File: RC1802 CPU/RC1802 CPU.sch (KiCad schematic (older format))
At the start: 50 parts, among them J1 Mount, J2 Mount, J3 Mount, J4 Mount, J5 CONN_01X39, J6 CONN_02X20, J7 BARREL_JACK, J8 Conn_CLK, J9 Conn_Q, U1 74LS04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

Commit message: Fixed label snafoos
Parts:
- removed J8: Conn_CLK, Pin_Headers:Pin_Header_Straight_1x05_Pitch2.54mm, symbol Conn_01x05
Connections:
- net labels removed: CLEAR, LOAD, RUN, WAIT, ~WE
- wire segments 224 -> 197
- no-connect marks 12 -> 24
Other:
- moved on the sheet: R4, R5, R6, R7, U1C, U1D, U1E, U1F, X1

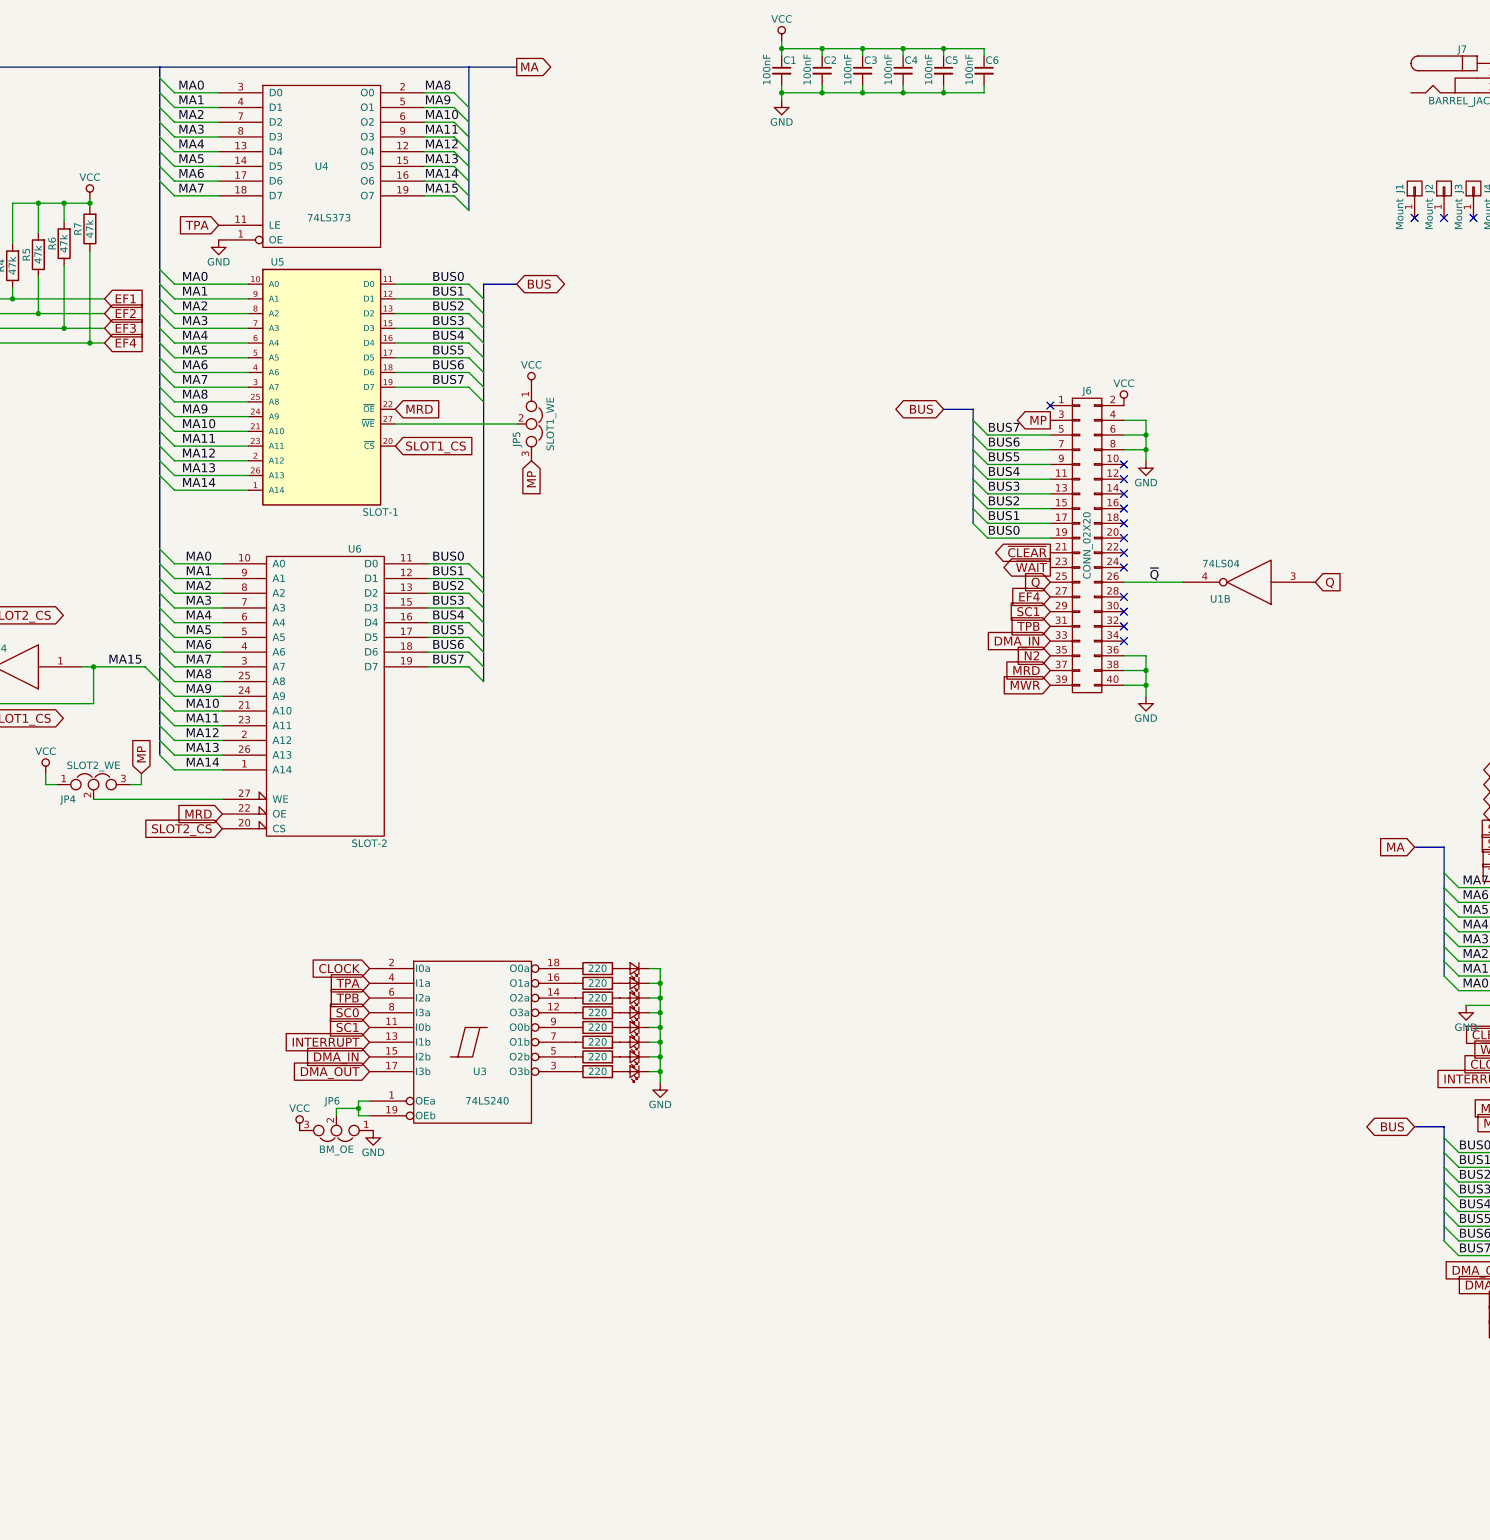
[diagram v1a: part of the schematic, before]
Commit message: Fixed tracks missing due to labelling issues
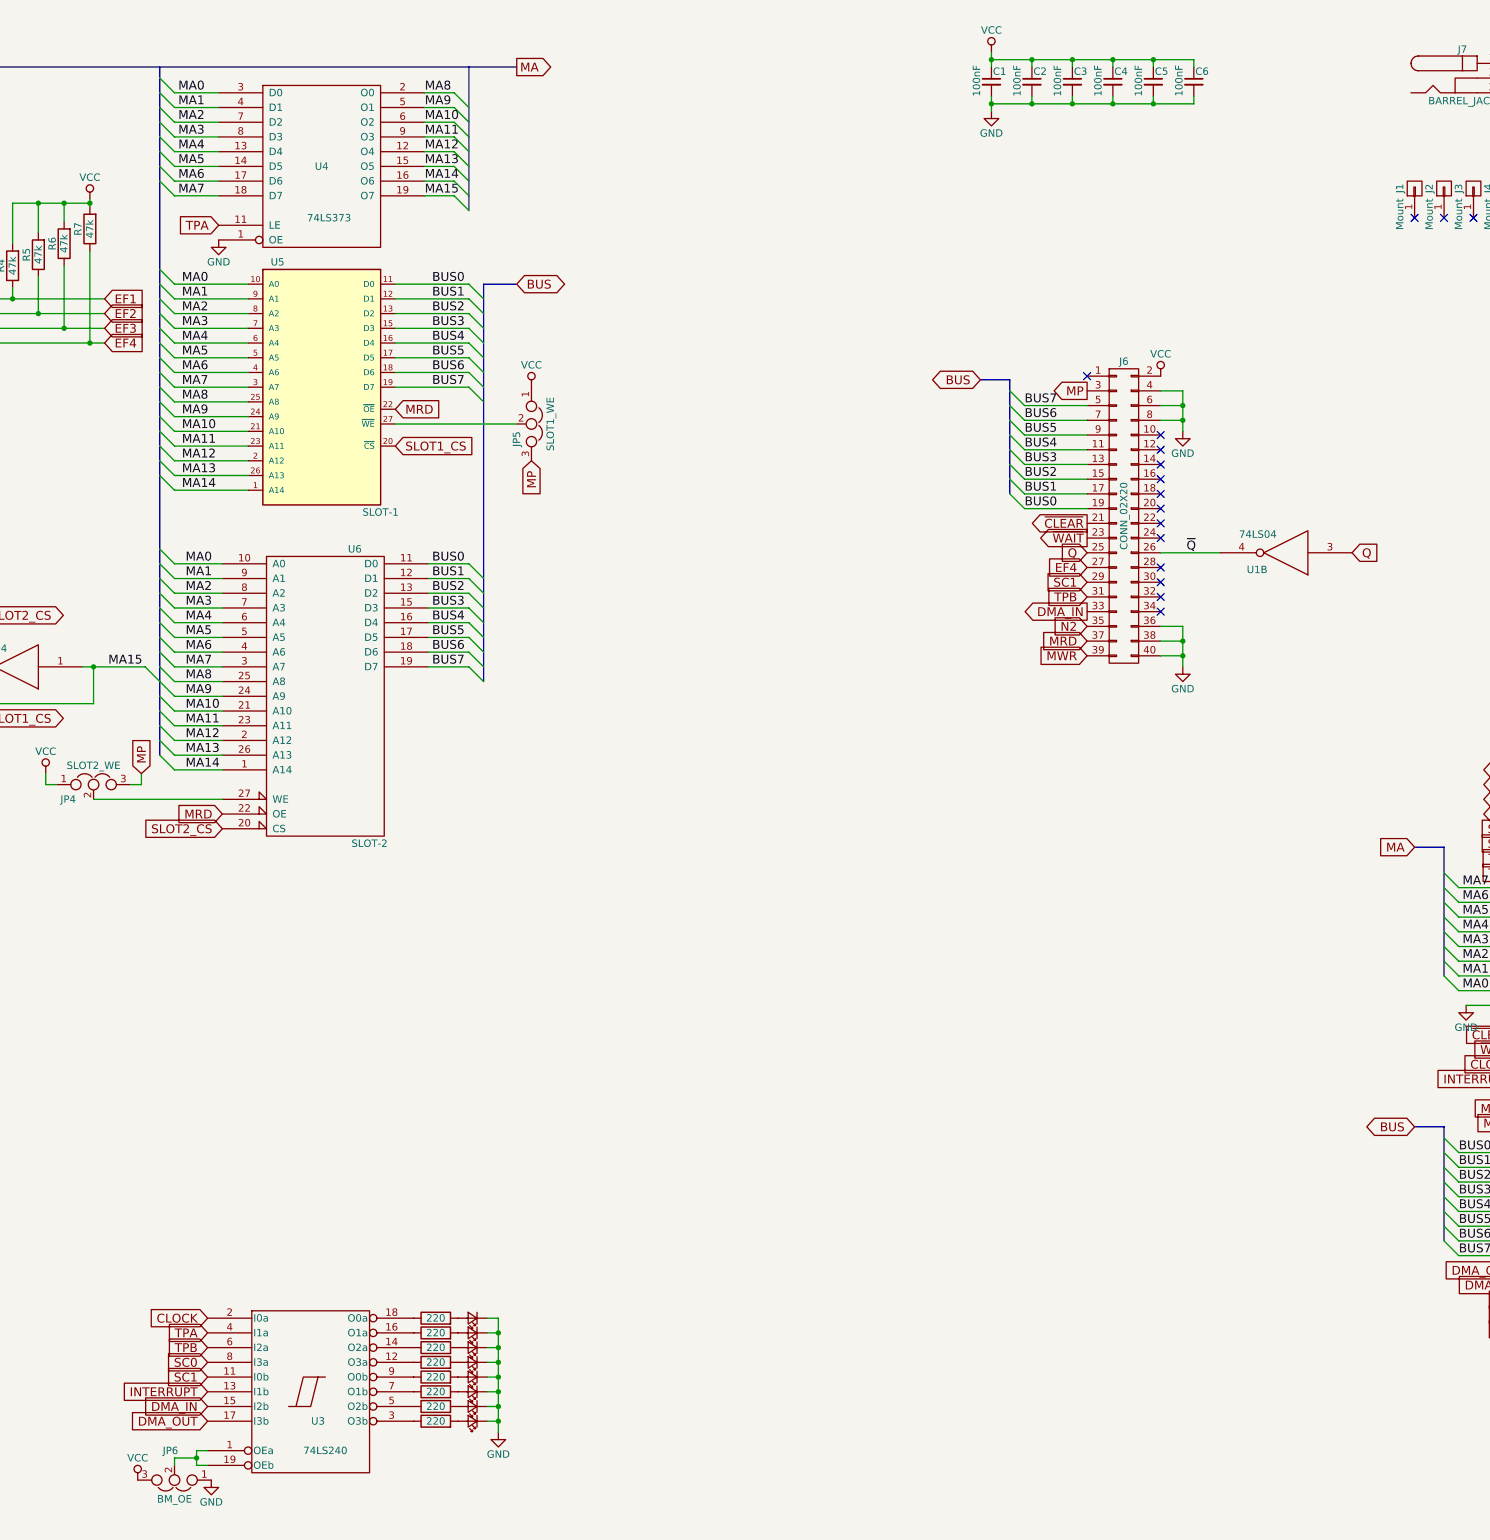
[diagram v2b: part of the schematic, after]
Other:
- moved on the sheet: C1, C2, C3, C4, C5, C6, J6, JP6, U1B, U3

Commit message: Gerber export CPU board after adding clockport
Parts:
- added J8: ClockPort, Pin_Headers:Pin_Header_Straight_1x05_Pitch2.54mm, symbol Conn_01x05-RESCUE-RC1802_CPU
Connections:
- net labels added: CLK_PWR
- wire segments 197 -> 205
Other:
- moved on the sheet: X1
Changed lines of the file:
@@
 EESchema Schematic File Version 2
+LIBS:RC1802 CPU-rescue
 LIBS:cdp1802
 LIBS:power
@@
 L CXO_DIP14 X1
 U 1 1 59462D89
-P 1225 1300
-F 0 "X1" H 1025 1550 50  0000 L CNN
-F 1 "CXO_DIP14" H 1275 1050 50  0000 L CNN
-F 2 "Oscillators:Oscillator_DIP-14" H 1675 950 50  0001 C CNN
-F 3 "" H 1125 1300 50  0001 C CNN
-	1    1225 1300
-	0    -1   1    0
+P 1800 1750
+F 0 "X1" H 1600 2000 50  0000 L CNN
+F 1 "CXO_DIP14" H 1850 1500 50  0000 L CNN
+F 2 "Oscillators:Oscillator_DIP-14" H 2250 1400 50  0001 C CNN
+F 3 "" H 1700 1750 50  0001 C CNN
+	1    1800 1750
+	-1   0    0    -1
 $EndComp
 $Comp
 L GND #PWR05
 U 1 1 59462F59
-P 1625 1400
-F 0 "#PWR05" H 1625 1150 50  0001 C CNN
-F 1 "GND" H 1625 1250 50  0000 C CNN
-F 2 "" H 1625 1400 50  0001 C CNN
-F 3 "" H 1625 1400 50  0001 C CNN
-	1    1625 1400
+P 1900 1075
+F 0 "#PWR05" H 1900 825 50  0001 C CNN
+F 1 "GND" H 1900 925 50  0000 C CNN
+F 2 "" H 1900 1075 50  0001 C CNN
+F 3 "" H 1900 1075 50  0001 C CNN
+	1    1900 1075
 	1    0    0    -1
 $EndComp
@@
 	1    0    0    -1
 $EndComp
-NoConn ~ 1225 1000
+NoConn ~ 2100 1750
 Text GLabel 15575 5900 0    60   Output ~ 0
 EF1
@@
 Text Label 8125 2000 0    60   ~ 0
 MA15
-Text GLabel 1225 1600 3    60   Output ~ 0
+Text GLabel 1500 1175 0    60   Output ~ 0
 CLOCK
 Text GLabel 3425 1550 0    60   Input ~ 0
@@
 L VCC #PWR024
 U 1 1 5BA993FE
-P 825 1200
-F 0 "#PWR024" H 825 1050 50  0001 C CNN
-F 1 "VCC" H 825 1350 50  0000 C CNN
-F 2 "" H 825 1200 50  0001 C CNN
-F 3 "" H 825 1200 50  0001 C CNN
-	1    825  1200
-	1    0    0    -1
-$EndComp
-Wire Wire Line
-	825  1200 825  1300
-Wire Wire Line
-	825  1300 925  1300
-Wire Wire Line
-	1525 1300 1625 1300
-Wire Wire Line
-	1625 1300 1625 1400
+P 2350 950
+F 0 "#PWR024" H 2350 800 50  0001 C CNN
+F 1 "VCC" H 2350 1100 50  0000 C CNN
+F 2 "" H 2350 950 50  0001 C CNN
+F 3 "" H 2350 950 50  0001 C CNN
+	1    2350 950
+	1    0    0    -1
+$EndComp
 Wire Wire Line
 	925  2825 925  2900
 Wire Wire Line
 	925  2825 1150 2825
+$Comp
+L Conn_01x05-RESCUE-RC1802_CPU J8
+U 1 1 5BA8B962
+P 1900 825
+F 0 "J8" H 1900 1125 50  0000 C CNN
+F 1 "ClockPort" H 1900 525 50  0000 C CNN
+F 2 "Pin_Headers:Pin_Header_Straight_1x05_Pitch2.54mm" H 1900 825 50  0001 C CNN
+F 3 "" H 1900 825 50  0001 C CNN
+	1    1900 825
+	0    -1   -1   0
+$EndComp
+Wire Wire Line
+	1800 1450 1800 1400
+Wire Wire Line
+	1800 1400 2000 1400
+Wire Wire Line
+	2000 1400 2000 1025
+Wire Wire Line
+	1500 1750 1500 1300
+Wire Wire Line
+	1500 1300 1800 1300
+Wire Wire Line
+	1800 1300 1800 1025
+Wire Wire Line
+	1500 1175 1700 1175
+Wire Wire Line
+	1700 1175 1700 1025
+Wire Wire Line
+	2350 950  2350 1175
+Wire Wire Line
+	2350 1175 2100 1175
+Wire Wire Line
+	2100 1175 2100 1025
+$Comp
+L GND #PWR025
+U 1 1 5BA8D417
+P 1800 2050
+F 0 "#PWR025" H 1800 1800 50  0001 C CNN
+F 1 "GND" H 1800 1900 50  0000 C CNN
+F 2 "" H 1800 2050 50  0001 C CNN
+F 3 "" H 1800 2050 50  0001 C CNN
+	1    1800 2050
+	1    0    0    -1
+$EndComp
+Text Label 1975 1400 2    60   ~ 0
+CLK_PWR
+Wire Wire Line
+	1900 1075 1900 1025
 $EndSCHEMATC

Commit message: Added jumpers for inverting TX/RX
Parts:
- removed J9: Conn_Q, Pin_Headers:Pin_Header_Angled_1x04_Pitch2.54mm, symbol Conn_01x04
- added D9: 1N4148, Diodes_THT:D_DO-35_SOD27_P7.62mm_Horizontal, symbol D
- added J9: Q_Connector, Pin_Headers:Pin_Header_Angled_1x05_Pitch2.54mm, symbol Conn_01x05_Male
- added JP1: RX_SEL, Pin_Headers:Pin_Header_Straight_1x03_Pitch2.54mm, symbol Jumper_NC_Dual
- added JP7: RX_INVERT, Pin_Headers:Pin_Header_Straight_1x03_Pitch2.54mm, symbol Jumper_NC_Dual
- added JP8: TX_INVERT, Pin_Headers:Pin_Header_Straight_1x03_Pitch2.54mm, symbol Jumper_NC_Dual
- J5: value CONN_01X39 -> Expansion
- J6: value CONN_02X20 -> UI_Connector
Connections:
- net labels added: RX, TX
- wire segments 205 -> 225
- no-connect marks 24 -> 23
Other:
- moved on the sheet: U1B, U1C
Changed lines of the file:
@@
 P 15775 7800
 F 0 "J5" H 15775 9800 50  0000 C CNN
-F 1 "CONN_01X39" V 15875 7800 50  0000 C CNN
+F 1 "Expansion" V 15875 7800 50  0000 C CNN
 F 2 "Pin_Headers:Pin_Header_Angled_1x39_Pitch2.54mm" H 15775 7800 50  0001 C CNN
 F 3 "" H 15775 7800 50  0001 C CNN
@@
 P 12875 4175
 F 0 "J6" H 12875 5225 50  0000 C CNN
-F 1 "CONN_02X20" V 12875 4175 50  0000 C CNN
+F 1 "UI_Connector" V 12875 4175 50  0000 C CNN
 F 2 "Pin_Headers:Pin_Header_Straight_2x20_Pitch2.54mm" H 12875 3225 50  0001 C CNN
 F 3 "" H 12875 3225 50  0001 C CNN
@@
 L 74LS04 U1
 U 2 1 5B22F8BE
-P 13975 4425
-F 0 "U1" H 14170 4540 50  0000 C CNN
-F 1 "74LS04" H 14165 4300 50  0000 C CNN
-F 2 "Housings_DIP:DIP-14_W7.62mm_Socket" H 13975 4425 50  0001 C CNN
-F 3 "" H 13975 4425 50  0001 C CNN
-	2    13975 4425
-	-1   0    0    1
+P 4050 8775
+F 0 "U1" H 4245 8890 50  0000 C CNN
+F 1 "74LS04" H 4240 8650 50  0000 C CNN
+F 2 "Housings_DIP:DIP-14_W7.62mm_Socket" H 4050 8775 50  0001 C CNN
+F 3 "" H 4050 8775 50  0001 C CNN
+	2    4050 8775
+	1    0    0    -1
 $EndComp
 $Comp
 L 74LS04 U1
 U 3 1 5B22F92F
-P 1175 9400
-F 0 "U1" H 1370 9515 50  0000 C CNN
-F 1 "74LS04" H 1365 9275 50  0000 C CNN
-F 2 "Housings_DIP:DIP-14_W7.62mm_Socket" H 1175 9400 50  0001 C CNN
-F 3 "" H 1175 9400 50  0001 C CNN
-	3    1175 9400
+P 4050 7075
+F 0 "U1" H 4245 7190 50  0000 C CNN
+F 1 "74LS04" H 4240 6950 50  0000 C CNN
+F 2 "Housings_DIP:DIP-14_W7.62mm_Socket" H 4050 7075 50  0001 C CNN
+F 3 "" H 4050 7075 50  0001 C CNN
+	3    4050 7075
 	-1   0    0    1
 $EndComp
@@
 	-1   0    0    1
 $EndComp
-NoConn ~ 725  9400
 NoConn ~ 725  9800
 NoConn ~ 725  10200
@@
 	1    0    0    -1
 $EndComp
-$Comp
-L Conn_01x04 J9
-U 1 1 5B6A11D6
-P 1350 3100
-F 0 "J9" H 1350 3200 50  0000 C CNN
-F 1 "Conn_Q" H 1350 2900 50  0000 C CNN
-F 2 "Pin_Headers:Pin_Header_Angled_1x04_Pitch2.54mm" H 1350 3100 50  0001 C CNN
-F 3 "" H 1350 3100 50  0001 C CNN
-	1    1350 3100
-	0    1    1    0
-$EndComp
-Text GLabel 1450 2825 1    60   Input ~ 0
+Text GLabel 1500 7275 3    60   Input ~ 0
 Q
 $Comp
 L GND #PWR021
 U 1 1 5B6A17C7
-P 925 2900
-F 0 "#PWR021" H 925 2650 50  0001 C CNN
-F 1 "GND" H 925 2750 50  0000 C CNN
-F 2 "" H 925 2900 50  0001 C CNN
-F 3 "" H 925 2900 50  0001 C CNN
-	1    925  2900
-	1    0    0    -1
+P 925 7175
+F 0 "#PWR021" H 925 6925 50  0001 C CNN
+F 1 "GND" H 925 7025 50  0000 C CNN
+F 2 "" H 925 7175 50  0001 C CNN
+F 3 "" H 925 7175 50  0001 C CNN
+	1    925  7175
+	-1   0    0    1
 $EndComp
 $Comp
 L VCC #PWR022
 U 1 1 5B6A3EEC
-P 1350 2625
-F 0 "#PWR022" H 1350 2475 50  0001 C CNN
-F 1 "VCC" H 1350 2775 50  0000 C CNN
-F 2 "" H 1350 2625 50  0001 C CNN
-F 3 "" H 1350 2625 50  0001 C CNN
-	1    1350 2625
-	1    0    0    -1
-$EndComp
-Text GLabel 1250 2825 1    60   Output ~ 0
-EF3
+P 1600 7425
+F 0 "#PWR022" H 1600 7275 50  0001 C CNN
+F 1 "VCC" H 1600 7575 50  0000 C CNN
+F 2 "" H 1600 7425 50  0001 C CNN
+F 3 "" H 1600 7425 50  0001 C CNN
+	1    1600 7425
+	-1   0    0    1
+$EndComp
 Wire Wire Line
 	4825 1600 4950 1600
@@
 	11975 1375 13350 1375
 Wire Wire Line
-	1775 9400 1775 10850
+	1775 9800 1775 10850
 Wire Wire Line
 	1775 10600 1625 10600
@@
 Connection ~ 1775 10200
 Wire Wire Line
-	1625 9800 1775 9800
-Connection ~ 1775 9800
-Wire Wire Line
 	7925 3550 8750 3550
 Wire Wire Line
@@
 	5550 6000 5550 5925
 Wire Wire Line
-	1450 2825 1450 2900
-Wire Wire Line
-	1150 2825 1150 2900
-Wire Wire Line
-	1350 2900 1350 2625
-Wire Wire Line
-	1250 2900 1250 2825
-Wire Wire Line
-	13125 4425 13525 4425
-Text GLabel 14425 4425 2    60   Input ~ 0
+	1600 7150 1600 7425
+Text GLabel 3350 8400 0    60   Input ~ 0
 Q
-Wire Wire Line
-	1625 9400 1775 9400
-Text Label 13300 4425 0    60   ~ 0
-~Q
 Wire Wire Line
 	13275 5125 13125 5125
@@
 $EndComp
 Wire Wire Line
-	925  2825 925  2900
-Wire Wire Line
-	925  2825 1150 2825
+	925  7250 925  7175
 $Comp
 L Conn_01x05-RESCUE-RC1802_CPU J8
@@
 Wire Wire Line
 	1900 1075 1900 1025
+Text GLabel 4850 8775 2    60   Output ~ 0
+~Q
+Text GLabel 13125 4425 2    60   Input ~ 0
+~Q
+Wire Wire Line
+	3350 8400 3500 8400
+$Comp
+L Jumper_NC_Dual JP1
+U 1 1 5BB50981
+P 2725 7450
+F 0 "JP1" H 2775 7350 50  0000 L CNN
+F 1 "RX_SEL" H 2725 7550 50  0000 C BNN
+F 2 "Pin_Headers:Pin_Header_Straight_1x03_Pitch2.54mm" H 2725 7450 50  0001 C CNN
+F 3 "" H 2725 7450 50  0001 C CNN
+	1    2725 7450
+	0    -1   -1   0
+$EndComp
+Text GLabel 2600 7075 0    60   Output ~ 0
+EF3
+Text GLabel 2600 7825 0    60   Output ~ 0
+EF4
+$Comp
+L D D9
+U 1 1 5BB522A5
+P 3100 7450
+F 0 "D9" H 3100 7550 50  0000 C CNN
+F 1 "1N4148" H 3100 7350 50  0000 C CNN
+F 2 "Diodes_THT:D_DO-35_SOD27_P7.62mm_Horizontal" H 3100 7450 50  0001 C CNN
+F 3 "" H 3100 7450 50  0001 C CNN
+	1    3100 7450
+	-1   0    0    1
+$EndComp
+Wire Wire Line
+	2950 7450 2825 7450
+$Comp
+L Jumper_NC_Dual JP7
+U 1 1 5BB52E45
+P 3475 7450
+F 0 "JP7" H 3525 7350 50  0000 L CNN
+F 1 "RX_INVERT" H 3475 7550 50  0000 C BNN
+F 2 "Pin_Headers:Pin_Header_Straight_1x03_Pitch2.54mm" H 3475 7450 50  0001 C CNN
+F 3 "" H 3475 7450 50  0001 C CNN
+	1    3475 7450
+	0    1    1    0
+$EndComp
+Wire Wire Line
+	3250 7450 3375 7450
+Wire Wire Line
+	3475 7200 3475 7075
+Wire Wire Line
+	3475 7075 3600 7075
+Wire Wire Line
+	3475 7700 3475 7825
+Wire Wire Line
+	4625 7825 3475 7825
+Wire Wire Line
+	4625 7075 4625 7825
+Wire Wire Line
+	4625 7075 4500 7075
+Wire Wire Line
+	4625 7450 4750 7450
+Connection ~ 4625 7450
+Wire Wire Line
+	2725 7200 2725 7075
+Wire Wire Line
+	2725 7075 2600 7075
+Wire Wire Line
+	2600 7825 2725 7825
+Wire Wire Line
+	2725 7825 2725 7700
+Text GLabel 4750 7450 2    60   Input ~ 0
+RX
+Wire Wire Line
+	1625 9800 1775 9800
+Text GLabel 4850 8400 2    60   Output ~ 0
+TX
+Wire Wire Line
+	4850 8400 4725 8400
+$Comp
+L Jumper_NC_Dual JP8
+U 1 1 5BB57218
+P 4625 8400
+F 0 "JP8" H 4675 8300 50  0000 L CNN
+F 1 "TX_INVERT" H 4625 8500 50  0000 C BNN
+F 2 "Pin_Headers:Pin_Header_Straight_1x03_Pitch2.54mm" H 4625 8400 50  0001 C CNN
+F 3 "" H 4625 8400 50  0001 C CNN
+	1    4625 8400
+	0    -1   -1   0
+$EndComp
+Wire Wire Line
+	4625 8650 4625 8775
+Wire Wire Line
+	3500 8025 3500 8775
+Wire Wire Line
+	3500 8025 4625 8025
+Connection ~ 3500 8400
+Wire Wire Line
+	4625 8025 4625 8150
+Wire Wire Line
+	4500 8775 4850 8775
+Connection ~ 4625 8775
+Wire Wire Line
+	3500 8775 3600 8775
+$Comp
+L Conn_01x05_Male J9
+U 1 1 5BB62C4C
+P 1400 6950
+F 0 "J9" H 1400 7250 50  0000 C CNN
+F 1 "Q_Connector" V 1325 6950 50  0000 C CNN
+F 2 "Pin_Headers:Pin_Header_Angled_1x05_Pitch2.54mm" H 1400 6950 50  0001 C CNN
+F 3 "" H 1400 6950 50  0001 C CNN
+	1    1400 6950
+	0    1    1    0
+$EndComp
+Text GLabel 1400 7275 3    60   Input ~ 0
+TX
+Text GLabel 1300 7275 3    60   Output ~ 0
+RX
+Wire Wire Line
+	1500 7275 1500 7150
+Wire Wire Line
+	1400 7150 1400 7275
+Wire Wire Line
+	1300 7275 1300 7150
+Wire Wire Line
+	925  7250 1200 7250
+Wire Wire Line
+	1200 7250 1200 7150
 $EndSCHEMATC

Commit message: Wider power tracks and moved clockport
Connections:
- net GND: no longer J6.40 (P40), J6.8 (P8)
- net VCC: now also J6.40 (P40)
- no-connect marks 23 -> 24
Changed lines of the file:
@@
 Q
 Wire Wire Line
-	13275 5125 13125 5125
-Wire Wire Line
 	13275 4925 13275 5200
 Wire Wire Line
 	13275 5025 13125 5025
-Connection ~ 13275 5125
 Wire Wire Line
 	13275 4925 13125 4925
@@
 $EndComp
 Wire Wire Line
-	13275 3525 13125 3525
-Wire Wire Line
 	13275 3325 13275 3600
 Wire Wire Line
 	13275 3425 13125 3425
-Connection ~ 13275 3525
 Wire Wire Line
 	13275 3325 13125 3325
@@
 	3475 7700 3475 7825
 Wire Wire Line
-	4625 7825 3475 7825
-Wire Wire Line
-	4625 7075 4625 7825
+	3475 7825 4625 7825
+Wire Wire Line
+	4625 7825 4625 7075
 Wire Wire Line
 	4625 7075 4500 7075
@@
 Wire Wire Line
 	1200 7250 1200 7150
+NoConn ~ 13125 3525
+$Comp
+L VCC #PWR?
+U 1 1 5BC737DE
+P 13400 5125
+F 0 "#PWR?" H 13400 4975 50  0001 C CNN
+F 1 "VCC" H 13400 5275 50  0000 C CNN
+F 2 "" H 13400 5125 50  0001 C CNN
+F 3 "" H 13400 5125 50  0001 C CNN
+	1    13400 5125
+	1    0    0    -1
+$EndComp
+Wire Wire Line
+	13125 5125 13400 5125
 $EndSCHEMATC

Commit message: Added clock in and out to UI connector
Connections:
- net CLOCK: now also J6.34 (P34)
- net CLOCK_OUT: now reaches J8.2 (Pin_2), X1.8 (OUT)
- net CLOCK_OUT: now also J6.32 (P32)
- no-connect marks 24 -> 22
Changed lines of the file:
@@
 NoConn ~ 13125 4525
 NoConn ~ 13125 4625
-NoConn ~ 13125 4725
-NoConn ~ 13125 4825
 Text GLabel 8850 3800 3    60   Input ~ 0
 MP
@@
 	1500 1750 1500 1300
 Wire Wire Line
-	1500 1300 1800 1300
+	1425 1300 1800 1300
 Wire Wire Line
 	1800 1300 1800 1025
@@
 Wire Wire Line
 	13125 5125 13400 5125
+Text GLabel 13125 4825 2    60   Input ~ 0
+CLOCK
+Text GLabel 1425 1300 0    60   Output ~ 0
+CLOCK_OUT
+Connection ~ 1500 1300
+Text GLabel 13125 4725 2    60   Input ~ 0
+CLOCK_OUT
 $EndSCHEMATC
